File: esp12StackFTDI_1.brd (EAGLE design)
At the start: 31.5 x 30 mm, 35 parts, among them J02 470, J04 470, J05 470, J12 470, J13 470

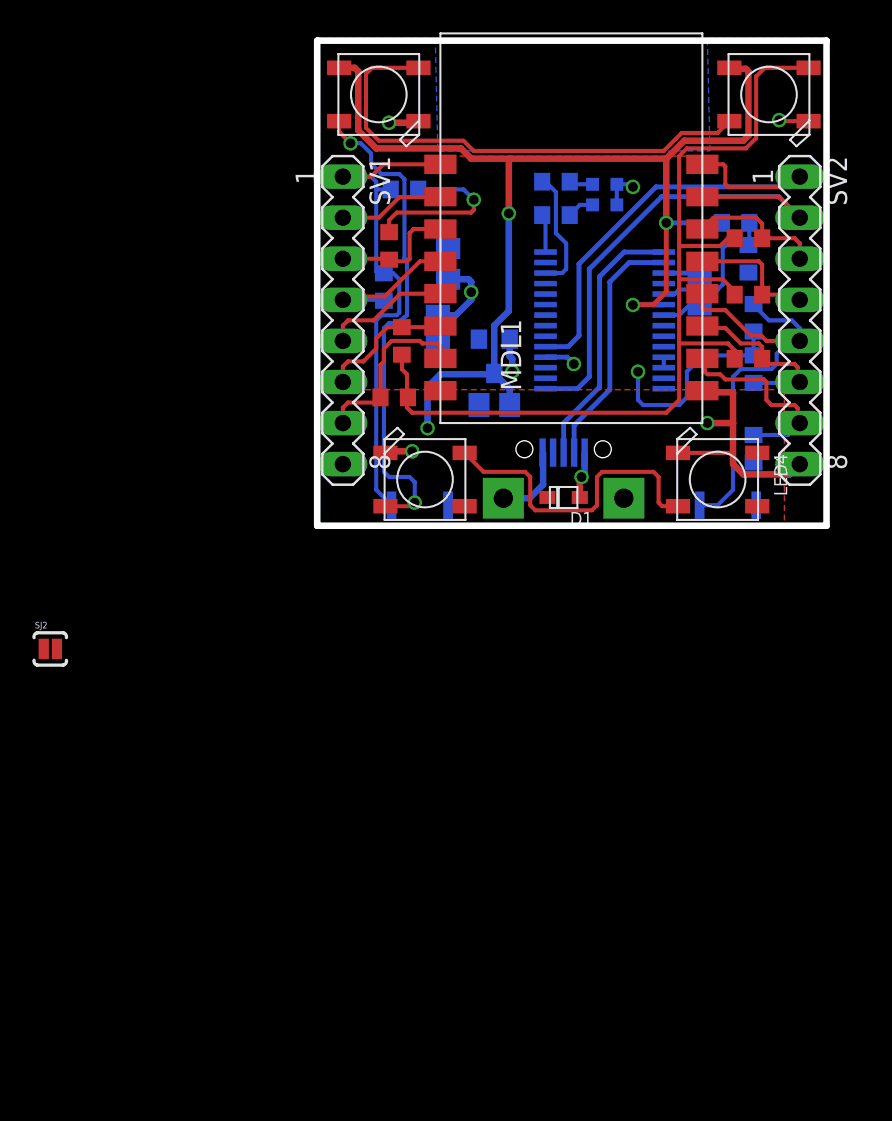
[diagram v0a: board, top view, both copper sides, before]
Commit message: FT232 module
FT232 Module now functional as a prototype
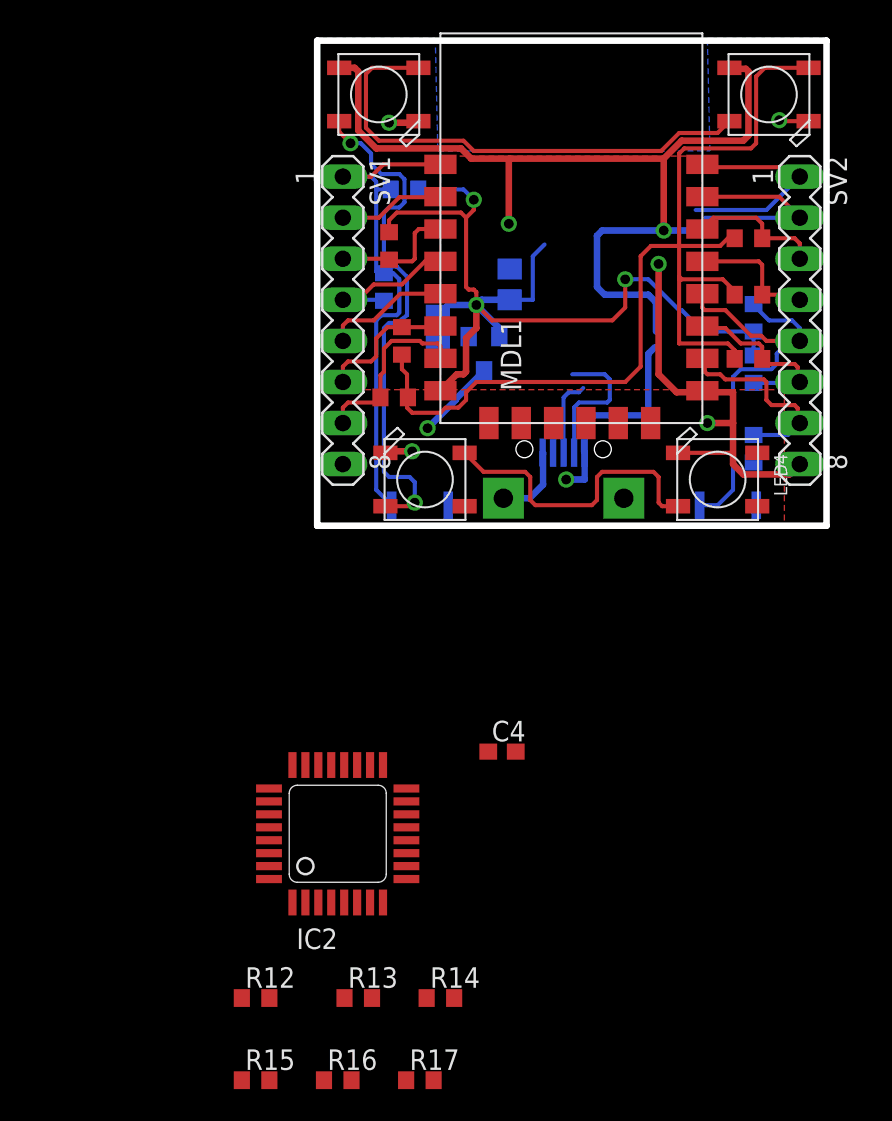
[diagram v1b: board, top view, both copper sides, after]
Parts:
- removed C5: 100nF, eagle-ltspice:C0805
- removed D1: (no value), adafruit:SOD-323F
- removed LED5, LED6: (no value), adafruit:CHIPLED_0603
- removed R10: 4k7, eagle-ltspice:R0603
- removed R11: 10k, eagle-ltspice:R0603
- removed R6, R7: (no value), rcl:R0603
- removed SJ2: SOLDERJUMPERNC2, SparkFun:SJ_2S-NOTRACE
- removed U1: (no value), ftdichip-4:SSOP28DB
- added IC2: (no value), FTDI:QFP-32
- added R12: 470R, eagle-ltspice:R0603
- added R13, R14: 27R, eagle-ltspice:R0603
- added R15: 1k4, eagle-ltspice:R0603
- added R16: 4k7, eagle-ltspice:R0603
- added R17: 10k, eagle-ltspice:R0603
- C4: value 10nF -> 33n; device eagle-ltspice:C0805 -> eagle-ltspice:C0603
- moved C4 21.4 mm to (11.4, -14.0), flipped to the top, turned to 0 degrees
- moved C2 4.02 mm to (11.9, 14.9)
- moved GND 0.65 mm to (10.3, 10.6)
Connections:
- removed net 3V3OUT: C5.2, U1.17
- removed net 5VUSB: D1.A, U$2.1
- removed net CBUS3: R6.2, U1.14
- removed net CBUS4: R7.1, U1.12
- removed net LED_RX: LED6.C, R7.2
- removed net LED_TX: LED5.C, R6.1
- removed net RESET: R10.2, R11.1, U1.19
- new net 3V3OUT1: C4.2, IC2.6
- new net AVCC1: IC2.30, R12.1
- new net RESET1: IC2.4, R16.2, R17.1
- new net RSTOUT1: IC2.5, R15.1
- new net USBDM1: IC2.8, R13.1
- new net USBDP1: IC2.7, R14.1, R15.2
- net 3V3: now also IC2.13, IC2.14; no longer LED5.A, LED6.A, U1.4
- net 5V: now also IC2.26, IC2.3, R12.2, R16.1, U$2.1; no longer C4.2, D1.C, R10.1, U1.20
- net D+: now also R14.2; no longer U1.15
- net D-: now also R13.2; no longer U1.16
- net DIN1: no longer SJ2.2
- net GND: now also IC2.17, IC2.29, IC2.9, R17.2; no longer C5.1, R11.2, U1.18, U1.21, U1.25, U1.26, U1.7
- net GPIO2: no longer SJ2.1
- net RXD: now also IC2.25; no longer U1.1
- net TXD: now also IC2.24; no longer U1.5
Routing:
- net 3V3: track 34.8 -> 58.1 mm, vias 6 -> 3
- net RXD: track 31.7 -> 12.4 mm
- net TXD: track 30.5 -> 13.6 mm
- net D+: track 16.4 -> 4.87 mm
- net RESET: track 9.19 -> 0.00 mm
- net CBUS4: track 7.52 -> 0.00 mm
- net GND: track 30.2 -> 37.0 mm, vias 4 -> 5
- net D-: track 15.3 -> 8.92 mm
- net DIN1: track 60.1 -> 65.2 mm
- net 5VUSB: track 3.23 -> 0.00 mm, vias 1 -> 0
- net 5V: track 74.8 -> 77.8 mm
- net CBUS3: track 2.37 -> 0.00 mm
- net 3V3OUT: track 2.25 -> 0.00 mm
- net DOUT2DIN3: track 30.7 -> 32.5 mm
- net LED_TX: track 1.68 -> 0.00 mm
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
